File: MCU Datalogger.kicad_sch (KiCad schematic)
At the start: 25 parts, among them U1 24LC1025, U2 24LC1025, U3 DS1337S_, U4 ATMEGA328P-AU, Y1 32.768 KHz, Y2 16 MHz

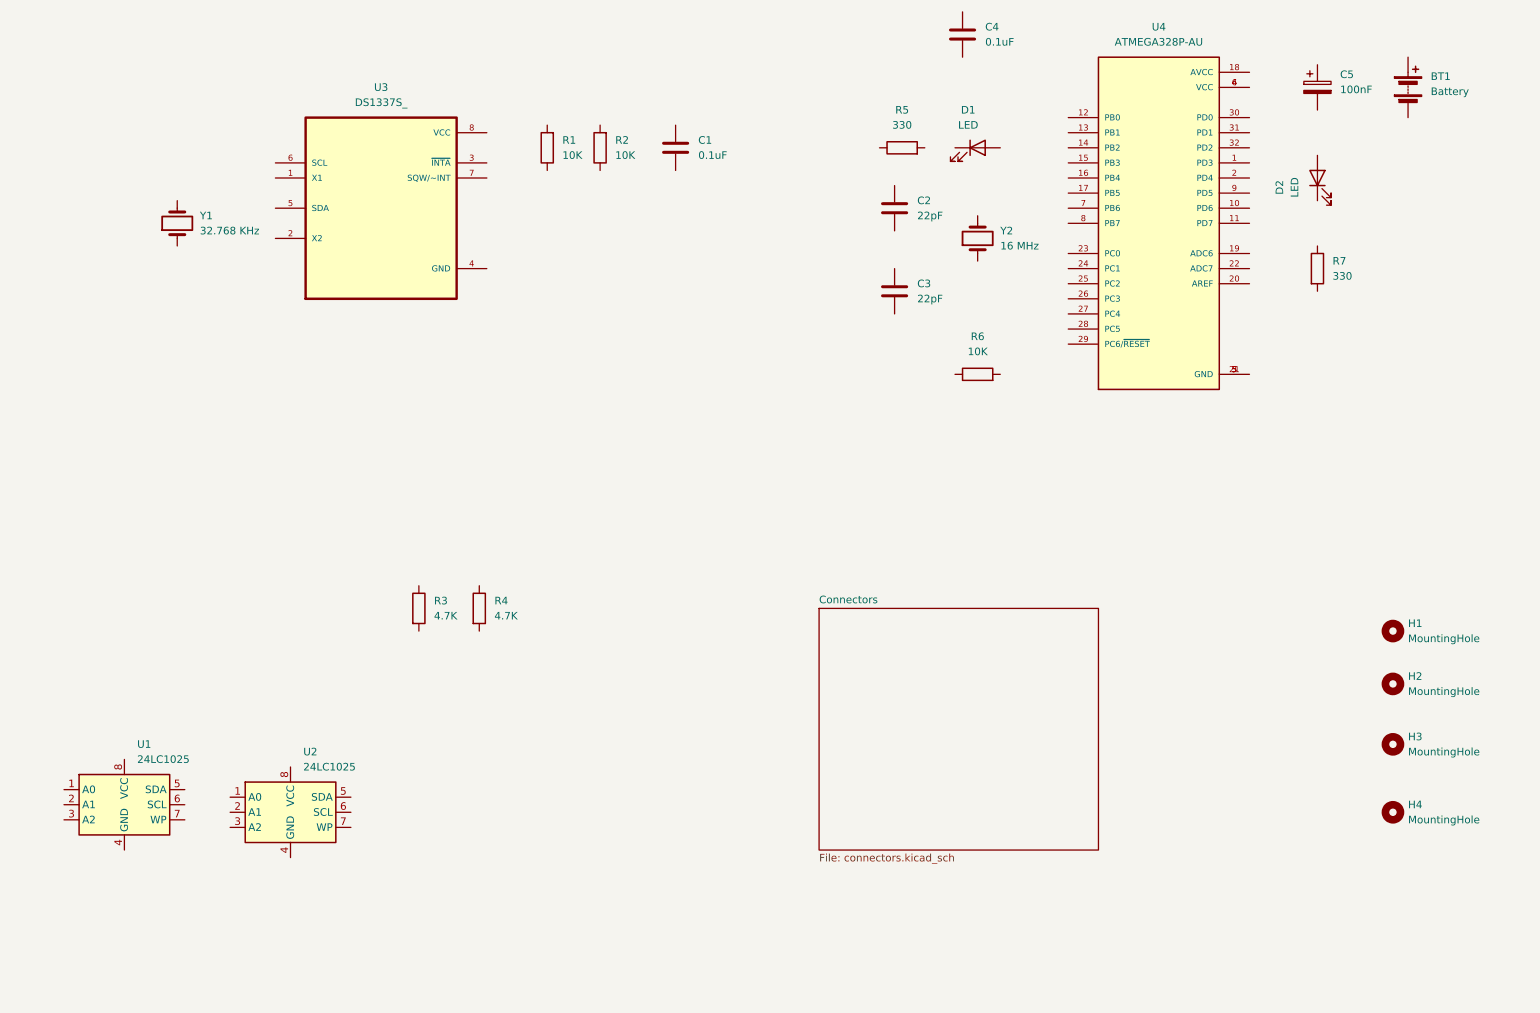
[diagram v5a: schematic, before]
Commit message: Wiring Main Sheet Completed
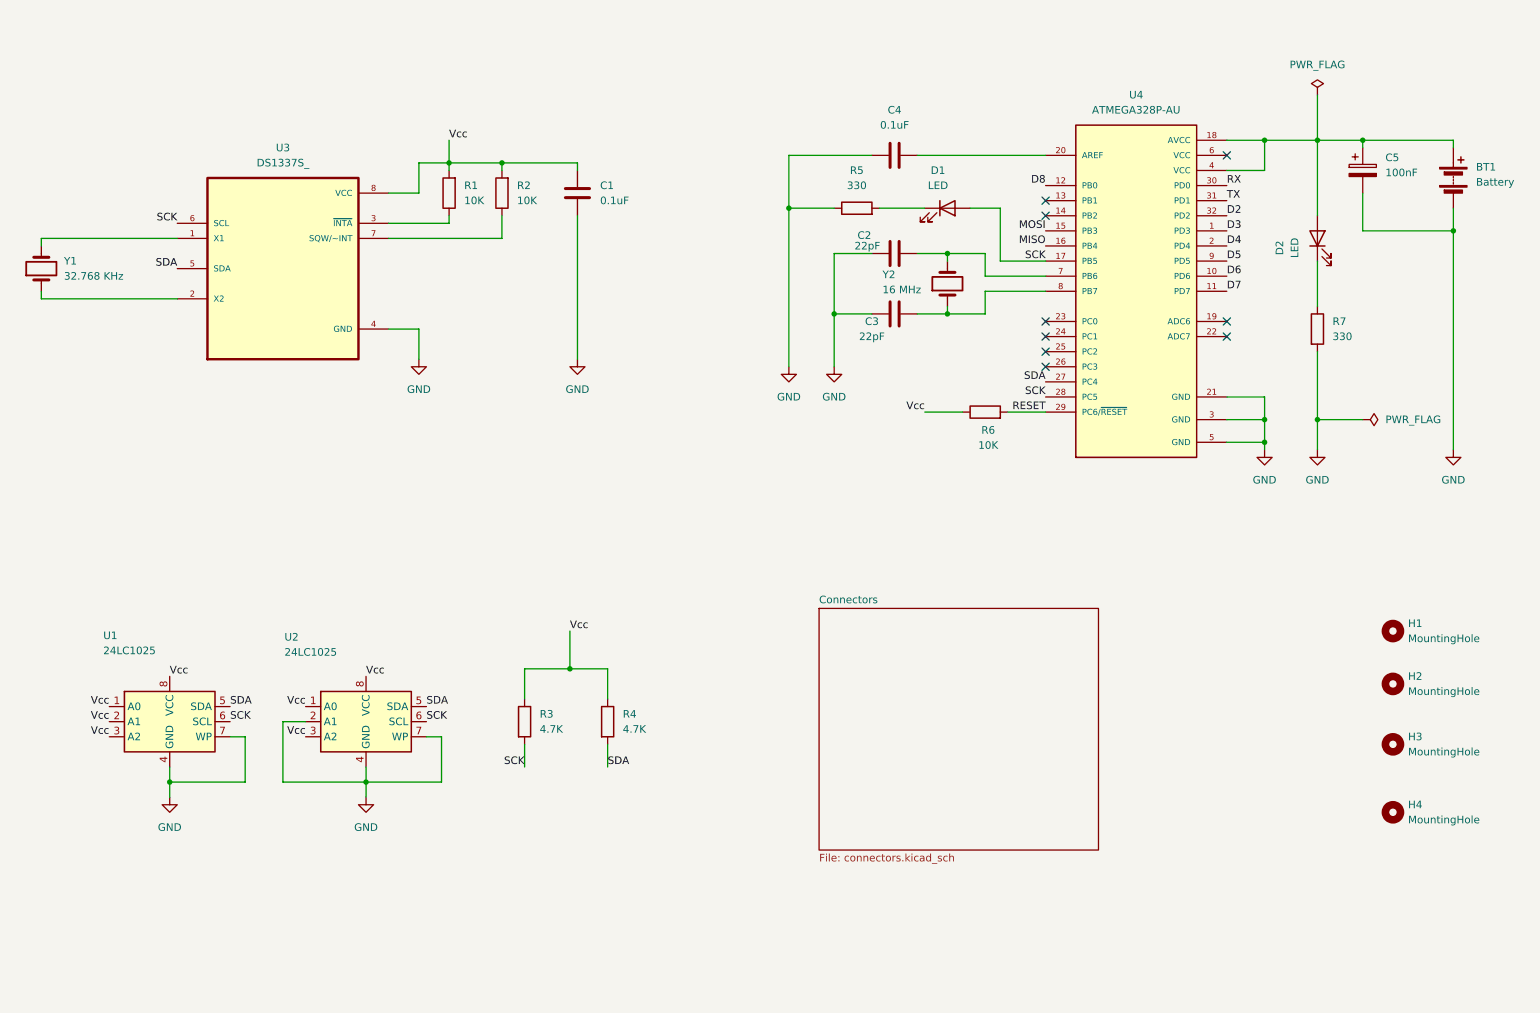
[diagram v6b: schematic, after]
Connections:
- net at BT1.1 (+): now also C5.1, D2.2 (A), U4.18 (AVCC), U4.4 (VCC)
- net GND: now reaches BT1.2 (-)
- net GND: now also C1.2, C2.1, C3.1, C4.1, C5.2, R5.1, R7.2, U1.4 (GND), U1.7 (WP), U2.2 (A1), U2.4 (GND), U2.7 (WP), U3.4 (GND), U4.21 (GND), U4.3 (GND), U4.5 (GND)
- net at D2.1 (K): now also R7.1
- net at R5.2: now also D1.1 (K)
- net at U3.1 (X1): now also Y1.2
- net at U3.2 (X2): now also Y1.1
- net at U3.3 (~{INTA}): now also R1.1
- net SDA: now reaches U3.5 (SDA)
- net SDA: now also R4.2, U1.5 (SDA), U2.5 (SDA), U4.27 (PC4)
- net SCK: now reaches U3.6 (SCL)
- net SCK: now also D1.2 (A), R3.2, U1.6 (SCL), U2.6 (SCL), U4.17 (PB5), U4.28 (PC5)
- net at U3.7 (SQW/~INT): now also R2.1
- net Vcc: now reaches U3.8 (VCC)
- net Vcc: now also C1.1, R1.2, R2.2, R3.1, R4.1, R6.1, U1.1 (A0), U1.2 (A1), U1.3 (A2), U1.8 (VCC), U2.1 (A0), U2.3 (A2), U2.8 (VCC)
- net D3: now reaches U4.1 (PD3)
- net D6: now reaches U4.10 (PD6)
- net D7: now reaches U4.11 (PD7)
- net D8: now reaches U4.12 (PB0)
- net MOSI: now reaches U4.15 (PB3)
- net MISO: now reaches U4.16 (PB4)
- net D4: now reaches U4.2 (PD4)
- net at U4.20 (AREF): now also C4.2
- net RESET: now reaches U4.29 (PC6/~{RESET})
- net RESET: now also R6.2
- net RX: now reaches U4.30 (PD0)
- net TX: now reaches U4.31 (PD1)
- net D2: now reaches U4.32 (PD2)
- net at U4.6 (VCC): no longer U4.4 (VCC)
- net at U4.7 (PB6): now also C2.2, Y2.2
- net at U4.8 (PB7): now also C3.2, Y2.1
- net D5: now reaches U4.9 (PD5)
- no-connect marks 0 -> 9
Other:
- moved on the sheet: BT1, C1, C2, C3, C4, C5, D1, D2, R1, R2, R3, R4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

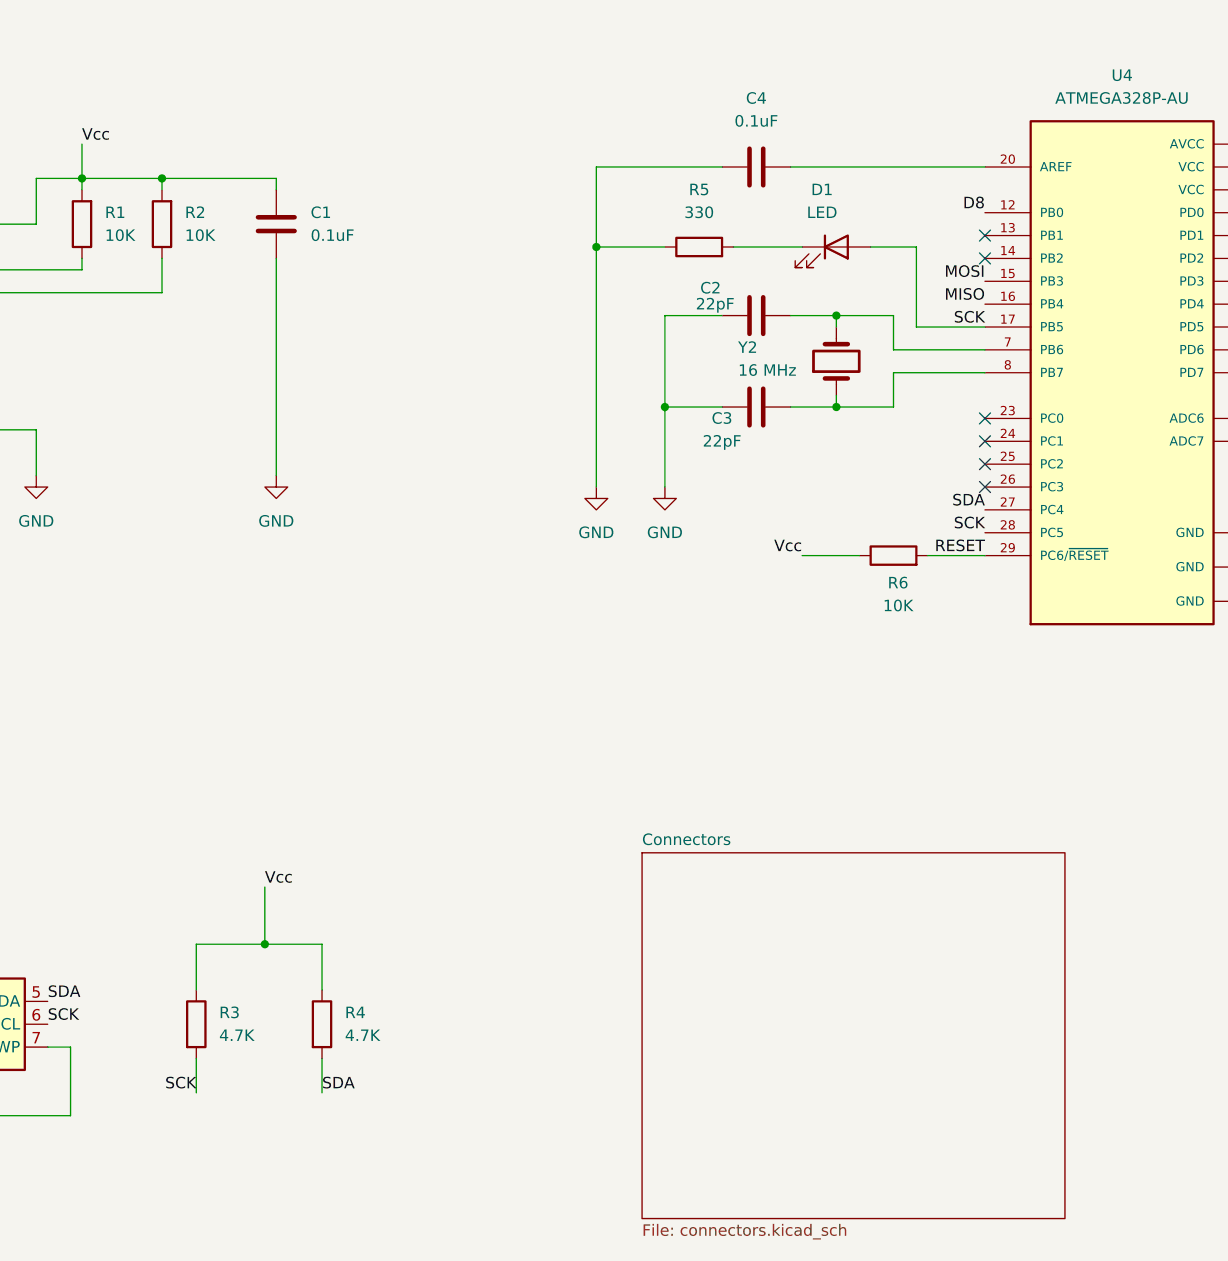
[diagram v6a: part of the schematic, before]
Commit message: Wiring Second Sheet Completed
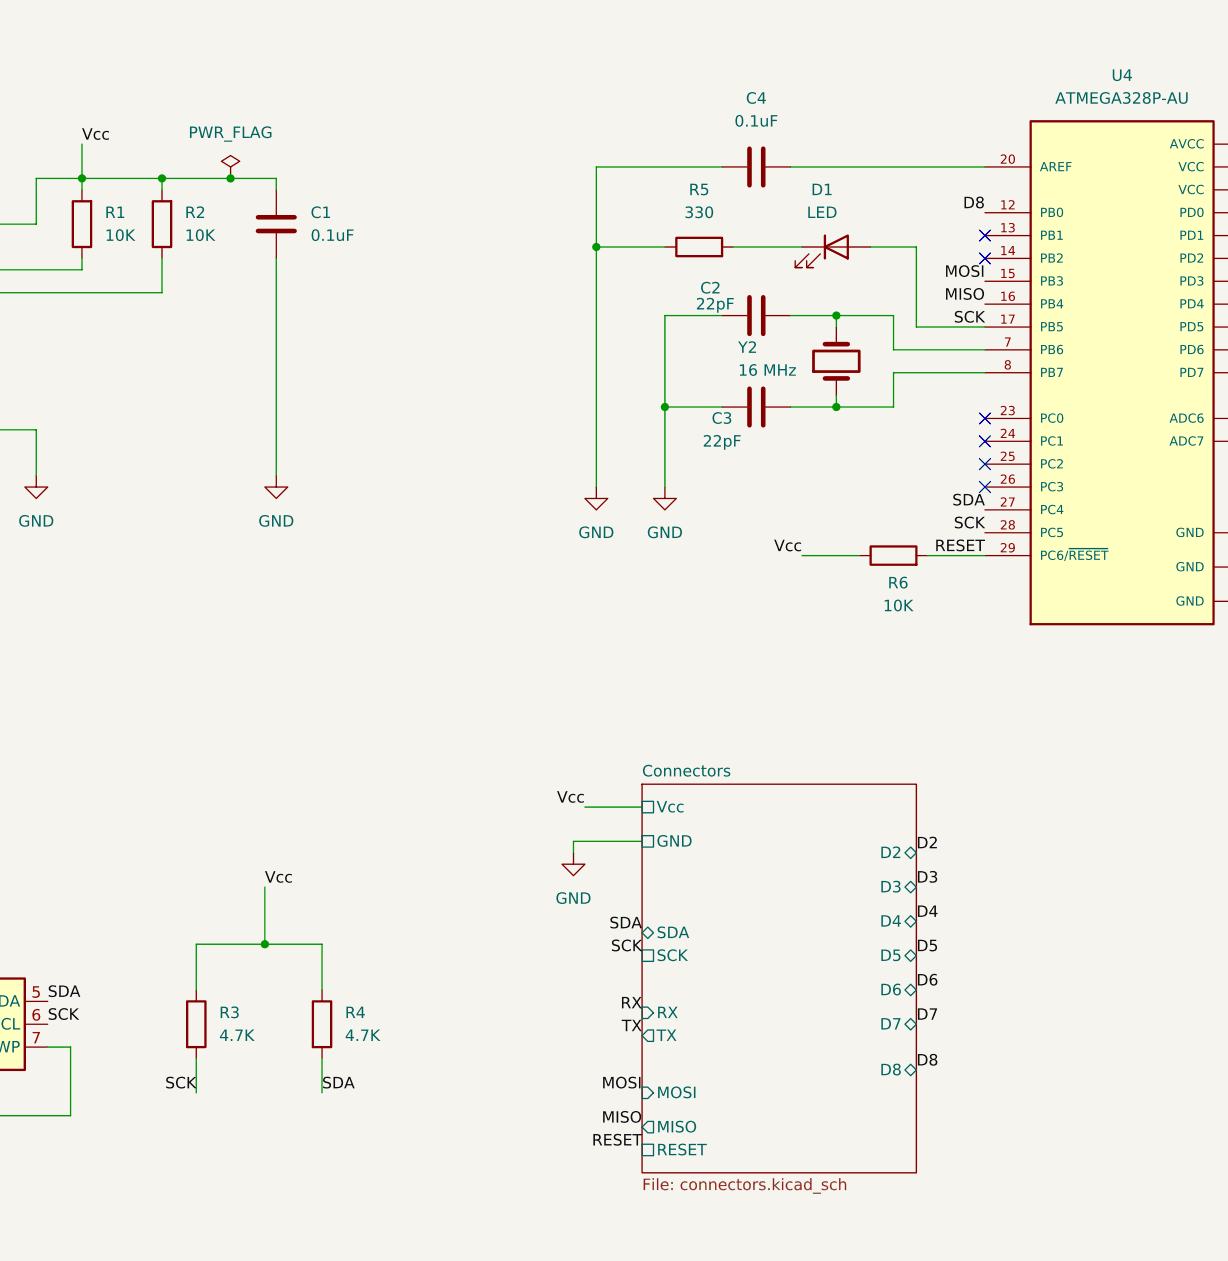
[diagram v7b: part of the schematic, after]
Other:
- sheet Connectors ports: added D2, D3, D4, D5, D6, D7, D8, GND, MISO, MOSI, RESET, RX, SCK, SDA, TX, Vcc; removed none
